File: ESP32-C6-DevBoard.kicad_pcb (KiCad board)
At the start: 2 copper layers, 62.2 x 30.5 mm, 49 parts, among them J1 USB_C_Receptacle_USB2.0_16P, J2 Conn_01x02_Pin, J4 USB_C_Receptacle_USB2.0_16P, J5 Conn_01x16_Pin, J6 Conn_01x16_Pin, Q1 BC847, Q2 BC847, U1 ESP32-C6-MINI-1, U2 CP2104, U3 TLV75801PDRV

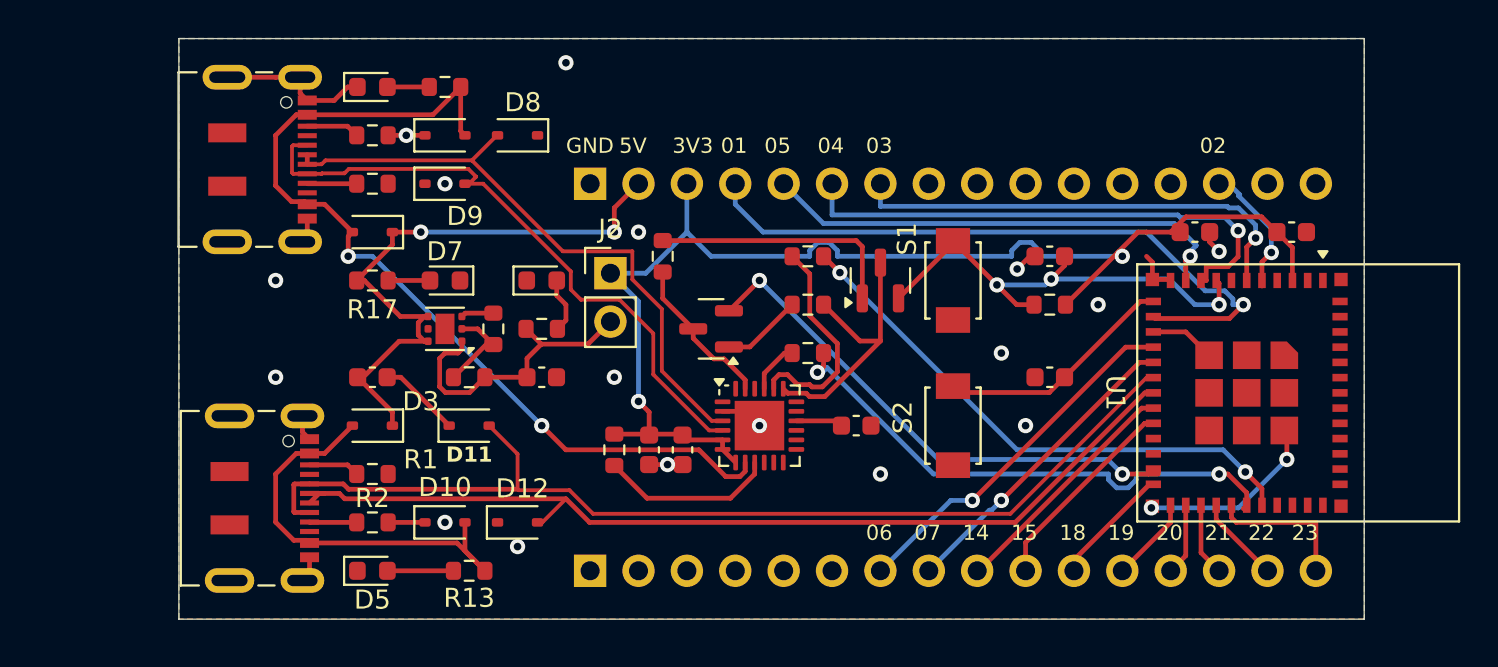
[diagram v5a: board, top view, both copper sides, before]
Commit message: Changed to better USB-C connector footprint. Reduced size Changed to 1A 3.3V converter
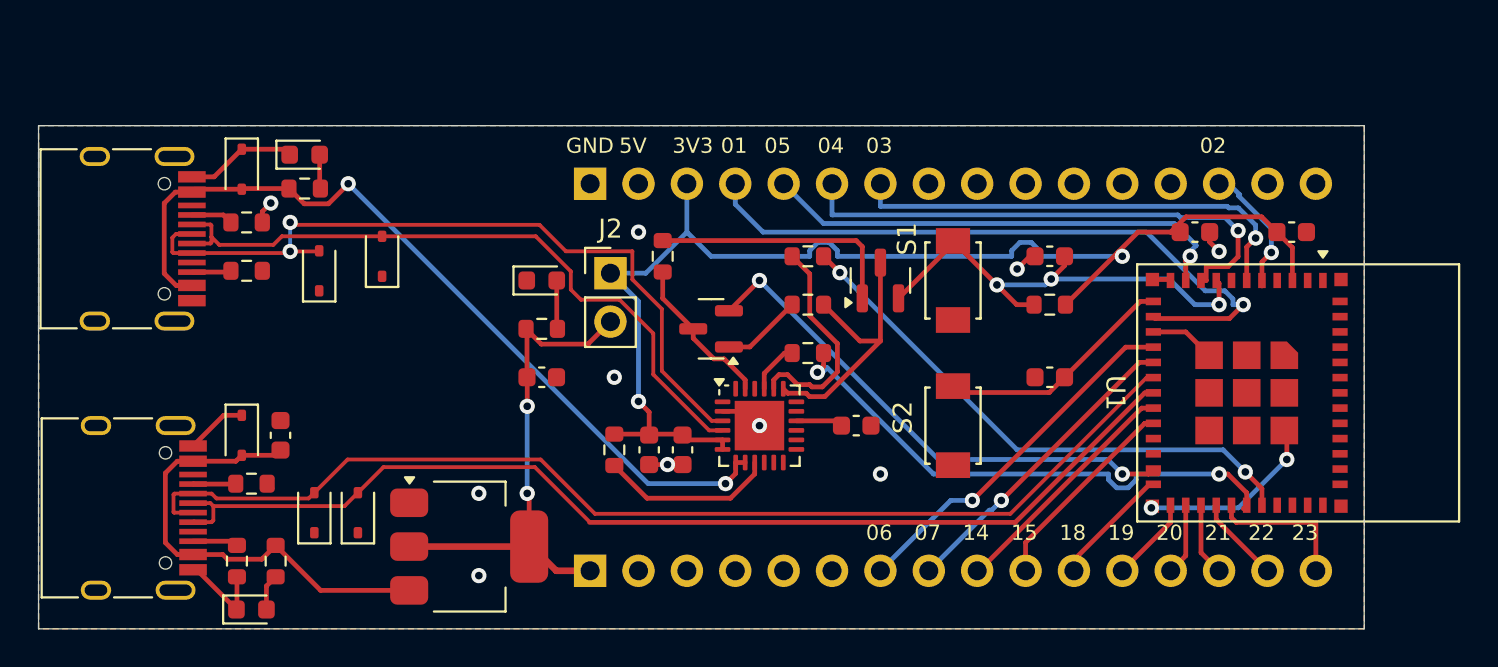
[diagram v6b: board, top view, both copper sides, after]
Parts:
- removed D2, D3: 1N5819WS, Diode_SMD:D_SOD-323
- removed D7: LED Yellow, LED_SMD:LED_0603_1608Metric
- removed R17: 470, Resistor_SMD:R_0603_1608Metric
- removed R3: 1M, Resistor_SMD:R_0603_1608Metric
- removed R4: 200k, Resistor_SMD:R_0603_1608Metric
- D1: value LED White -> LED Green
- D4: value LED Red -> LED Green
- J1, J4: footprint Connector_USB:USB_C_Receptacle_JAE_DX07S016JA1R1500 -> Connector_USB:USB_C_Receptacle_HRO_TYPE-C-31-M-12
- R13, R15: value 470 -> 620
- R5: value 51 -> 100
- U3: value TLV75801PDRV -> TLV76133DCY; footprint Package_SON:WSON-6-1EP_2x2mm_P0.65mm_EP1x1.6mm -> Package_TO_SOT_SMD:SOT-223-3_TabPin2
- moved D8 12.6 mm to (92.5, 59.2), turned to 90 degrees
- moved D10 11.6 mm to (88.4, 67.8), turned to -90 degrees
- moved U3 11.5 mm to (100.3, 73.7), turned to 0 degrees
- moved D6 10.8 mm to (88.4, 53.8), turned to -90 degrees
- moved R13 10.2 mm to (90.2, 74.4), turned to -90 degrees
- moved D11 9.33 mm to (92.2, 71.9), turned to 90 degrees
- moved R15 9.09 mm to (91.7, 54.9), turned to 0 degrees
- moved D12 8.40 mm to (94.5, 71.9), turned to 90 degrees
- moved J4 8.19 mm to (81.7, 57.5)
- moved R7 8.03 mm to (88.6, 56.6)
- moved R8 8.03 mm to (88.6, 59.2)
- moved R2 7.40 mm to (88.1, 74.4), turned to -90 degrees
- moved J1 7.13 mm to (81.8, 71.6)
- moved D5 6.67 mm to (88.9, 77.0)
- moved R1 6.37 mm to (88.9, 70.4)
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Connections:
- C2 pad 1: Net-(J2-Pin_2) -> /PWR_3V3_PRE
- D10 pad 2: /PWR_USB1_VBUS -> /PWR_5V
- J1 pad A4: /PWR_USB1_VBUS -> /PWR_5V
- J1 pad A9: /PWR_USB1_VBUS -> /PWR_5V
- J1 pad B4: /PWR_USB1_VBUS -> /PWR_5V
- J1 pad B9: /PWR_USB1_VBUS -> /PWR_5V
- J2 pad 2: Net-(J2-Pin_2) -> /PWR_3V3_PRE
- J5 pad 1: unconnected-(J5-Pin_1-Pad1) -> /PWR_3V3_PRE
- J6 pad 2: /PWR_5V -> unconnected-(J6-Pin_2-Pad2)
- R13 pad 1: /PWR_USB1_VBUS -> /PWR_5V
- R5 pad 1: Net-(J2-Pin_2) -> /PWR_3V3_PRE
- U2 pad 7: /PWR_3V3 -> /PWR_USB2_VBUS
- U3 pad 1: Net-(J2-Pin_2) -> GND
- U3 pad 2: Net-(U3-FB) -> /PWR_3V3_PRE
- U3 pad 3: GND -> /PWR_5V
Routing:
- net /PWR_3V3_PRE: track 0.00 -> 27.0 mm, vias 0 -> 2
- net /PWR_USB1_VBUS: track 22.6 -> 0.00 mm
- net Net-(J2-Pin_2): track 15.7 -> 0.00 mm
- net GND: track 44.7 -> 36.4 mm, vias 19 -> 12
- net /USB2_P: track 32.7 -> 41.0 mm, vias 0 -> 2
- net /PWR_5V: track 32.3 -> 25.1 mm, vias 2 -> 0
- net /USB1_P: track 50.7 -> 57.3 mm
- net Net-(U3-FB): track 4.80 -> 0.00 mm
- net /PWR_USB2_VBUS: track 48.7 -> 44.3 mm
- net /USB1_N: track 55.0 -> 58.5 mm
- net /USB2_N: track 33.6 -> 36.2 mm
- net Net-(D7-A): track 2.20 -> 0.00 mm
- net Net-(D5-A): track 3.47 -> 1.91 mm
- net /PWR_3V3: track 66.4 -> 65.4 mm
- net Net-(J4-CC1): track 2.79 -> 2.21 mm
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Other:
- board size 62.2 x 30.5 mm -> 69.6 x 26.4 mm

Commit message: Further improvements
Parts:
- moved J2 1.65 mm to (107.7, 61.0)
- moved R11 1.27 mm to (111.8, 58.4)
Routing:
- net /USB2_N: track 36.2 -> 38.6 mm
- net /USB2_P: track 41.0 -> 42.5 mm
- net Net-(Q1-B): track 13.3 -> 12.1 mm
- net /DTR: track 8.24 -> 7.71 mm
- net GND: vias 12 -> 16

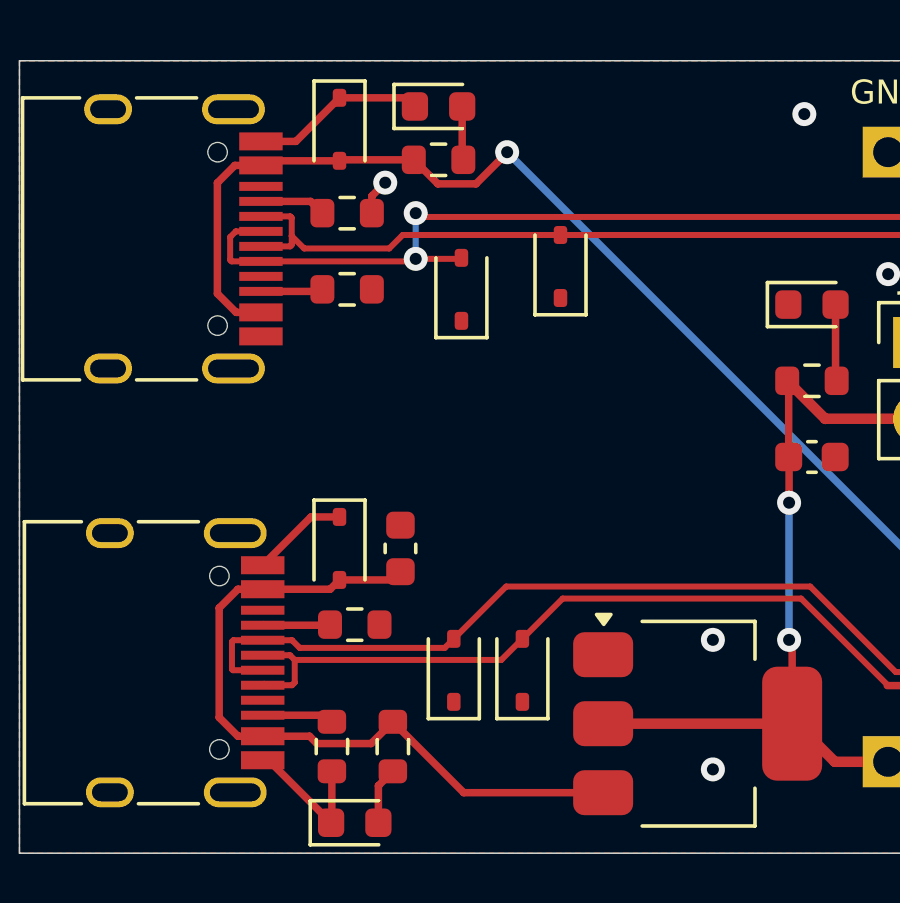
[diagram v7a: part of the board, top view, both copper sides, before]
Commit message: Change to unidirectional diodes (as that is what I actuallt ordered)
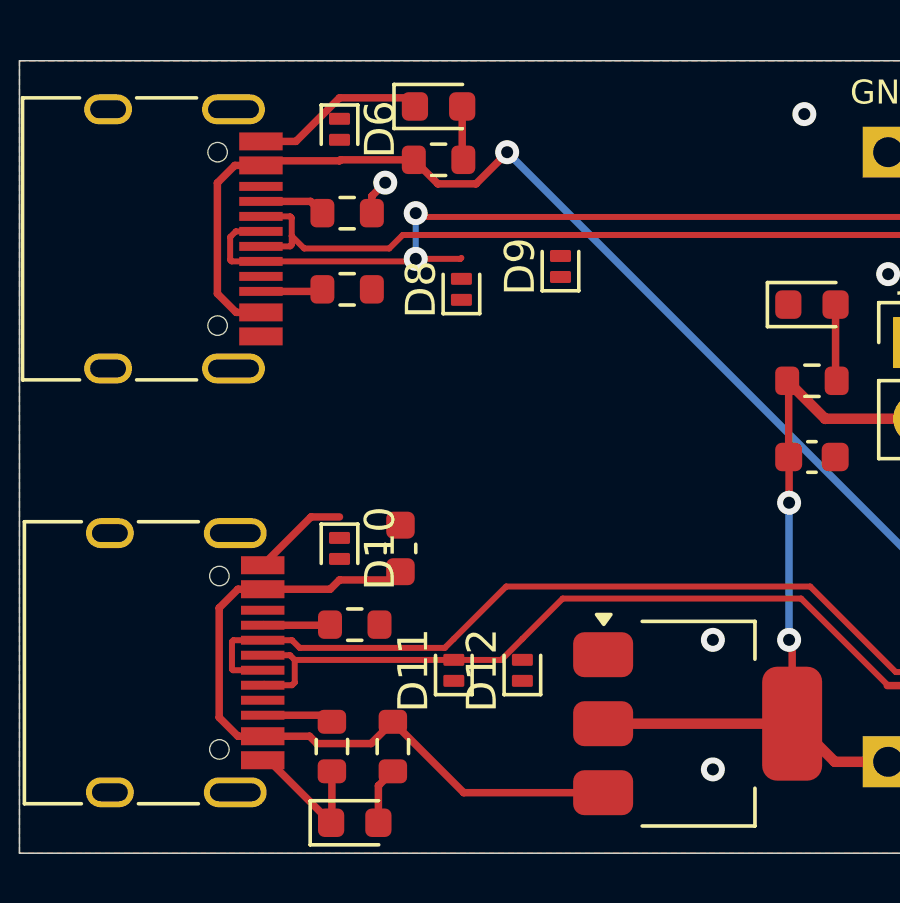
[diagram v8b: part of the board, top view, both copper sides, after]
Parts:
- D10, D11, D12, D6, D8, D9: footprint Diode_SMD:D_SOD-323 -> Diode_SMD:D_SOD-882
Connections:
- D10 pad 1: GND -> /PWR_5V
- D10 pad 2: /PWR_5V -> GND
- D11 pad 1: GND -> /USB1_N
- D11 pad 2: /USB1_N -> GND
- D12 pad 1: GND -> /USB1_P
- D12 pad 2: /USB1_P -> GND
- D6 pad 1: GND -> /PWR_USB2_VBUS
- D6 pad 2: /PWR_USB2_VBUS -> GND
- D8 pad 1: GND -> /USB2_P
- D8 pad 2: /USB2_P -> GND
- D9 pad 1: GND -> /USB2_N
- D9 pad 2: /USB2_N -> GND
